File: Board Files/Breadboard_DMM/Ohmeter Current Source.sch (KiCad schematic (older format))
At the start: 18 parts

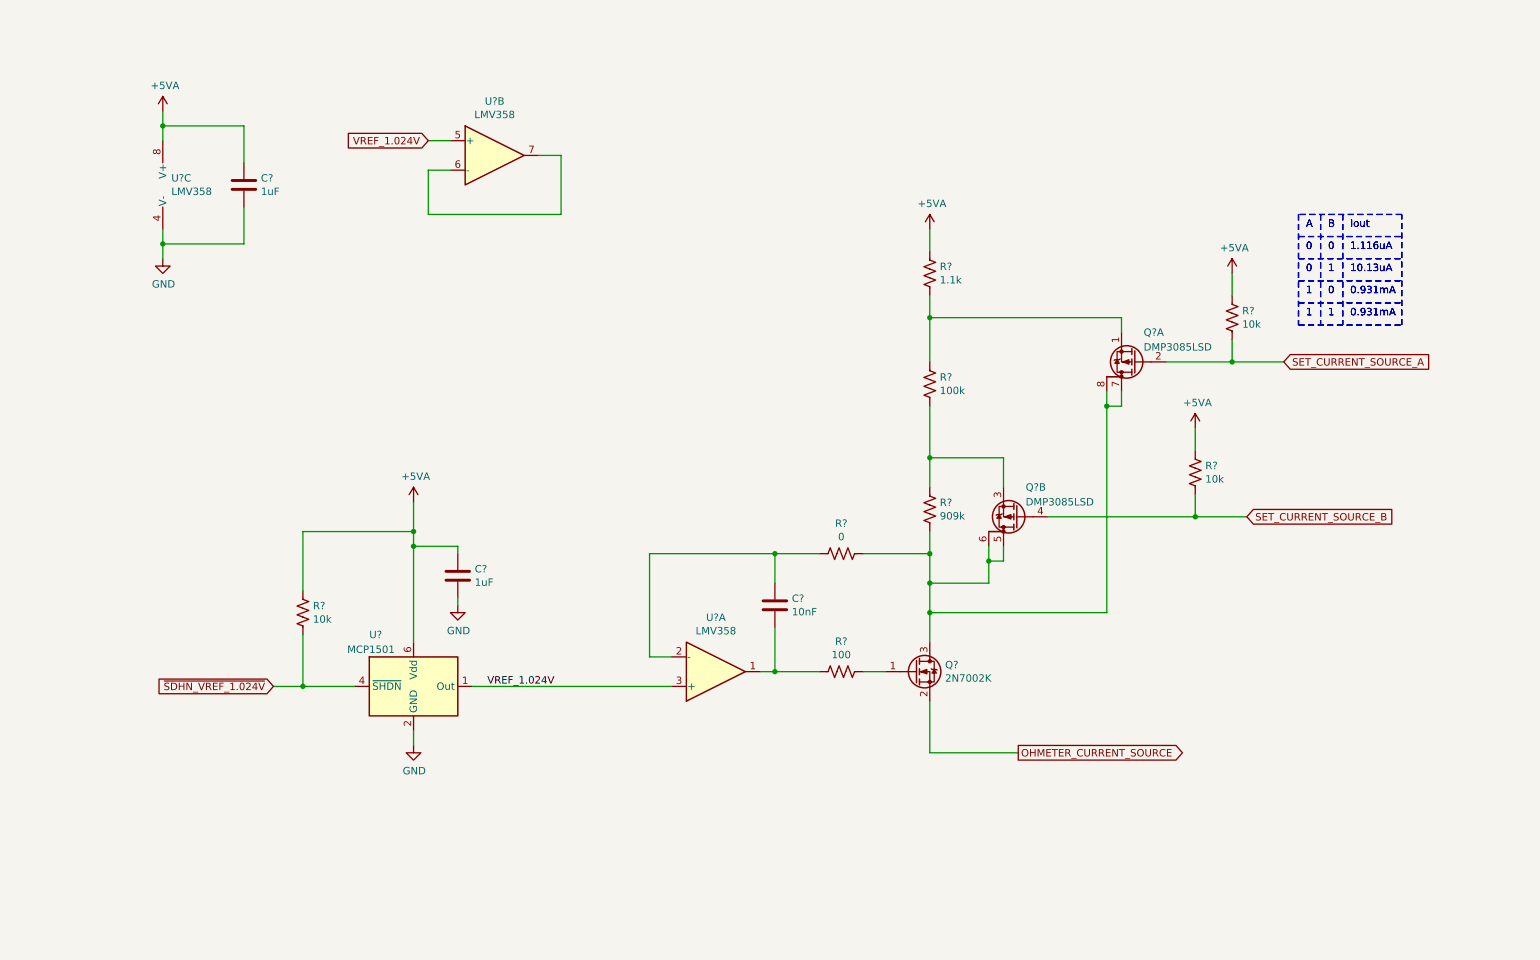
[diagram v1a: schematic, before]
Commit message: Starting converting to hierachichal design
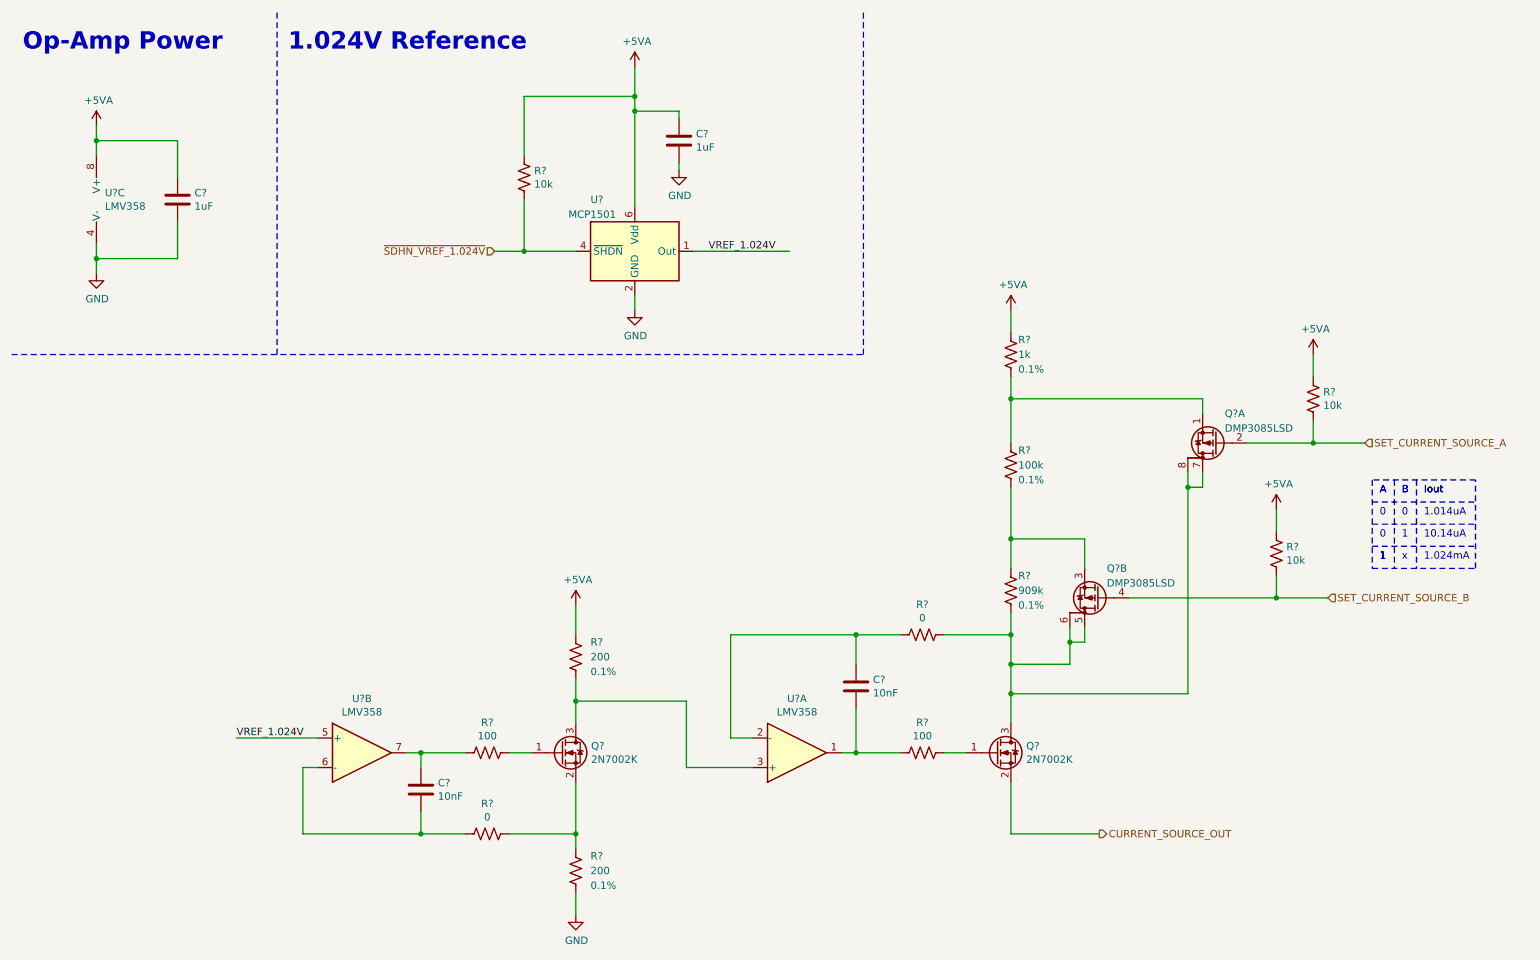
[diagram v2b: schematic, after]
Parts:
- added C?: 10nF, symbol Device:C
- added Q?: 2N7002K, Package_TO_SOT_SMD:SOT-23, symbol Transistor_FET:2N7002K
- added R?: 100, symbol Device:R_US
- added R?: 0, symbol Device:R_US
- added R? (x2): 200, symbol Device:R_US
- R?: value 1.1k -> 1k; Tolerance (none) -> 0.1%
- R? (x2): Tolerance (none) -> 0.1%
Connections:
- net +5VA: now also R?.1
- net GND: now also R?.2
- net VREF_1.024V: no longer U?.3 (+)
- net at U?.6 (-): now also C?.2, R?.2; no longer U?.7
- net OHMETER_CURRENT_SOURCE renamed CURRENT_SOURCE_OUT
- new net: C?.1, R?.2, U?.7
- new net: Q?.3 (D), R?.2, U?.3 (+)
- new net: Q?.1 (G), R?.1
- new net: Q?.2 (S), R?.1, R?.1
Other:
- note added: "1.014uA"
- note added: "1.024V Reference"
- note added: "1.024mA"
- note added: "10.14uA"
- note added: "Op-Amp Power"
- note added: "x"
- note removed: "0.931mA"
- note removed: "1.116uA"
- note removed: "10.13uA"
- moved on the sheet: C?, Q?, Q?A, Q?B, R?, U?, U?A, U?B, U?C

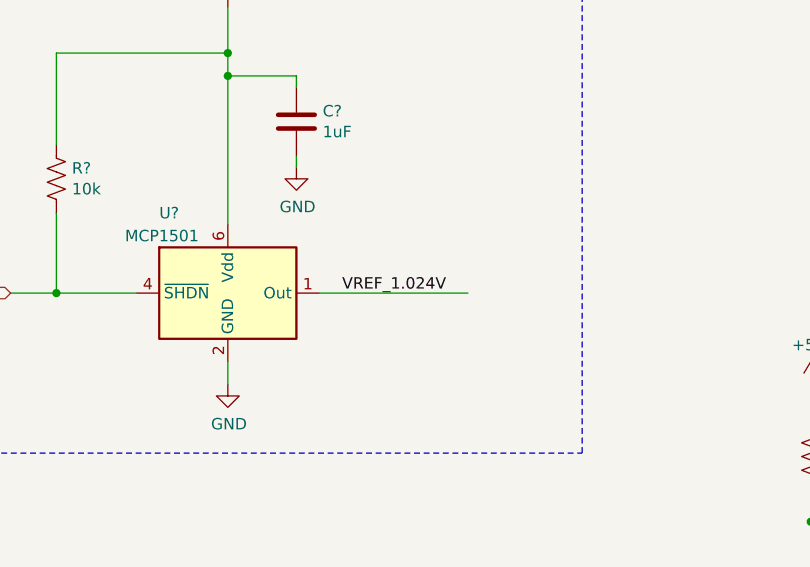
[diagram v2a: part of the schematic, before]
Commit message: Added new sheet for main supply measurement, added upgrades document
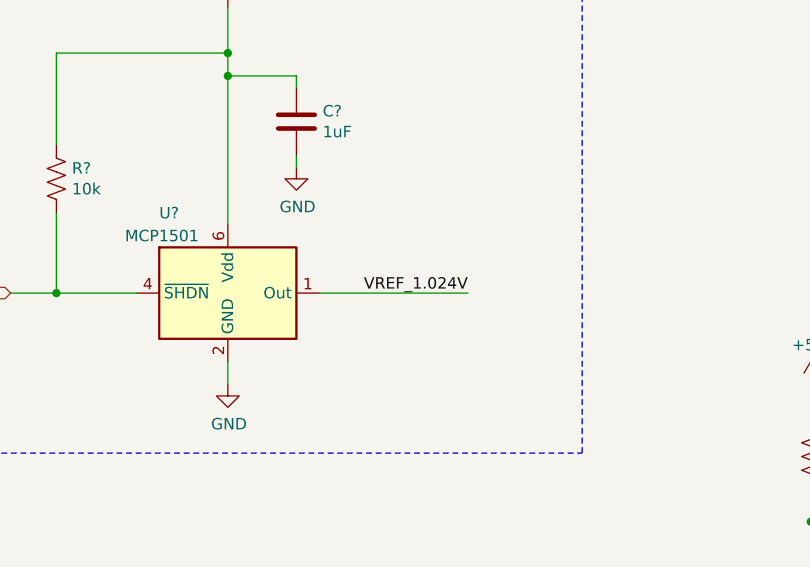
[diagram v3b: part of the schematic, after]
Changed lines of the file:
@@
 AR Path="/5F511849/5F51AF3B" Ref="U?"  Part="3"
 AR Path="/5F5089CB/5F51AF3B" Ref="U?"  Part="3"
+AR Path="/5F7E5DD1/5F51AF3B" Ref="U?"  Part="3"
+AR Path="/5F511849/5F7E68F4/5F51AF3B" Ref="U?"  Part="3"
 F 0 "U?" H 1108 1796 50  0000 L CNN
 F 1 "LMV358" H 1108 1705 50  0000 L CNN
@@
 AR Path="/5F511849/5F51AF41" Ref="C?"  Part="1"
 AR Path="/5F5089CB/5F51AF41" Ref="C?"  Part="1"
+AR Path="/5F7E5DD1/5F51AF41" Ref="C?"  Part="1"
+AR Path="/5F511849/5F7E68F4/5F51AF41" Ref="C?"  Part="1"
 F 0 "C?" H 1715 1796 50  0000 L CNN
 F 1 "1uF" H 1715 1705 50  0000 L CNN
@@
 AR Path="/5F511849/5F51AF4D" Ref="#PWR?"  Part="1"
 AR Path="/5F5089CB/5F51AF4D" Ref="#PWR?"  Part="1"
+AR Path="/5F7E5DD1/5F51AF4D" Ref="#PWR?"  Part="1"
+AR Path="/5F511849/5F7E68F4/5F51AF4D" Ref="#PWR?"  Part="1"
 F 0 "#PWR?" H 1050 1100 50  0001 C CNN
 F 1 "+5VA" H 1065 1423 50  0000 C CNN
@@
 AR Path="/5F511849/5F51AF55" Ref="#PWR?"  Part="1"
 AR Path="/5F5089CB/5F51AF55" Ref="#PWR?"  Part="1"
+AR Path="/5F7E5DD1/5F51AF55" Ref="#PWR?"  Part="1"
+AR Path="/5F511849/5F7E68F4/5F51AF55" Ref="#PWR?"  Part="1"
 F 0 "#PWR?" H 1050 2000 50  0001 C CNN
 F 1 "GND" H 1055 2077 50  0000 C CNN
@@
 AR Path="/5F511849/5F51AF8E" Ref="U?"  Part="1"
 AR Path="/5F5089CB/5F51AF8E" Ref="U?"  Part="1"
+AR Path="/5F7E5DD1/5F51AF8E" Ref="U?"  Part="1"
+AR Path="/5F511849/5F7E68F4/5F51AF8E" Ref="U?"  Part="1"
 F 0 "U?" H 4400 2450 50  0000 L CNN
 F 1 "MCP1501" H 4250 2350 50  0000 L CNN
@@
 AR Path="/5F511849/5F51AF88" Ref="R?"  Part="1"
 AR Path="/5F5089CB/5F51AF88" Ref="R?"  Part="1"
+AR Path="/5F7E5DD1/5F51AF88" Ref="R?"  Part="1"
+AR Path="/5F511849/5F7E68F4/5F51AF88" Ref="R?"  Part="1"
 F 0 "R?" H 4018 1646 50  0000 L CNN
 F 1 "10k" H 4018 1555 50  0000 L CNN
@@
 AR Path="/5F511849/5F51AF7B" Ref="C?"  Part="1"
 AR Path="/5F5089CB/5F51AF7B" Ref="C?"  Part="1"
+AR Path="/5F7E5DD1/5F51AF7B" Ref="C?"  Part="1"
+AR Path="/5F511849/5F7E68F4/5F51AF7B" Ref="C?"  Part="1"
 F 0 "C?" H 5115 1396 50  0000 L CNN
 F 1 "1uF" H 5115 1305 50  0000 L CNN
@@
 AR Path="/5F511849/5F51AF75" Ref="#PWR?"  Part="1"
 AR Path="/5F5089CB/5F51AF75" Ref="#PWR?"  Part="1"
+AR Path="/5F7E5DD1/5F51AF75" Ref="#PWR?"  Part="1"
+AR Path="/5F511849/5F7E68F4/5F51AF75" Ref="#PWR?"  Part="1"
 F 0 "#PWR?" H 4700 2250 50  0001 C CNN
 F 1 "GND" H 4705 2327 50  0000 C CNN
@@
 AR Path="/5F511849/5F51AF6F" Ref="#PWR?"  Part="1"
 AR Path="/5F5089CB/5F51AF6F" Ref="#PWR?"  Part="1"
+AR Path="/5F7E5DD1/5F51AF6F" Ref="#PWR?"  Part="1"
+AR Path="/5F511849/5F7E68F4/5F51AF6F" Ref="#PWR?"  Part="1"
 F 0 "#PWR?" H 5000 1300 50  0001 C CNN
 F 1 "GND" H 5005 1377 50  0000 C CNN
@@
 AR Path="/5F511849/5F51AF64" Ref="#PWR?"  Part="1"
 AR Path="/5F5089CB/5F51AF64" Ref="#PWR?"  Part="1"
+AR Path="/5F7E5DD1/5F51AF64" Ref="#PWR?"  Part="1"
+AR Path="/5F511849/5F7E68F4/5F51AF64" Ref="#PWR?"  Part="1"
 F 0 "#PWR?" H 4700 700 50  0001 C CNN
 F 1 "+5VA" H 4715 1023 50  0000 C CNN
@@
 Wire Wire Line
 	4700 2400 4700 2500
-Text Label 5200 2100 0    50   ~ 0
+Text Label 5750 2100 2    50   ~ 0
 VREF_1.024V
 Wire Wire Line
@@
 AR Path="/5F511849/5F51AFA6" Ref="C?"  Part="1"
 AR Path="/5F5089CB/5F51AFA6" Ref="C?"  Part="1"
+AR Path="/5F7E5DD1/5F51AFA6" Ref="C?"  Part="1"
+AR Path="/5F511849/5F7E68F4/5F51AFA6" Ref="C?"  Part="1"
 F 0 "C?" H 6315 5096 50  0000 L CNN
 F 1 "10nF" H 6315 5005 50  0000 L CNN
@@
 AR Path="/5F511849/5F51AFB7" Ref="R?"  Part="1"
 AR Path="/5F5089CB/5F51AFB7" Ref="R?"  Part="1"
+AR Path="/5F7E5DD1/5F51AFB7" Ref="R?"  Part="1"
+AR Path="/5F511849/5F7E68F4/5F51AFB7" Ref="R?"  Part="1"
 F 0 "R?" V 6445 5500 50  0000 C CNN
 F 1 "100" V 6536 5500 50  0000 C CNN
@@
 AR Path="/5F511849/5F51AFBD" Ref="Q?"  Part="1"
 AR Path="/5F5089CB/5F51AFBD" Ref="Q?"  Part="1"
+AR Path="/5F7E5DD1/5F51AFBD" Ref="Q?"  Part="1"
+AR Path="/5F511849/5F7E68F4/5F51AFBD" Ref="Q?"  Part="1"
 F 0 "Q?" H 7354 5546 50  0000 L CNN
 F 1 "2N7002K" H 7354 5455 50  0000 L CNN
@@
 AR Path="/5F511849/5F51AFCA" Ref="R?"  Part="1"
 AR Path="/5F5089CB/5F51AFCA" Ref="R?"  Part="1"
+AR Path="/5F7E5DD1/5F51AFCA" Ref="R?"  Part="1"
+AR Path="/5F511849/5F7E68F4/5F51AFCA" Ref="R?"  Part="1"
 F 0 "R?" H 7300 3650 50  0000 L CNN
 F 1 "100k" H 7300 3550 50  0000 L CNN
@@
 AR Path="/5F511849/5F51AFD0" Ref="R?"  Part="1"
 AR Path="/5F5089CB/5F51AFD0" Ref="R?"  Part="1"
+AR Path="/5F7E5DD1/5F51AFD0" Ref="R?"  Part="1"
+AR Path="/5F511849/5F7E68F4/5F51AFD0" Ref="R?"  Part="1"
 F 0 "R?" H 7300 4500 50  0000 L CNN
 F 1 "909k" H 7300 4400 50  0000 L CNN
@@
 AR Path="/5F511849/5F51AFDC" Ref="U?"  Part="1"
 AR Path="/5F5089CB/5F51AFDC" Ref="U?"  Part="1"
+AR Path="/5F7E5DD1/5F51AFDC" Ref="U?"  Part="1"
+AR Path="/5F511849/5F7E68F4/5F51AFDC" Ref="U?"  Part="1"
 F 0 "U?" H 5800 5133 50  0000 C CNN
 F 1 "LMV358" H 5800 5224 50  0000 C CNN
@@
 AR Path="/5F511849/5F51AFAC" Ref="R?"  Part="1"
 AR Path="/5F5089CB/5F51AFAC" Ref="R?"  Part="1"
+AR Path="/5F7E5DD1/5F51AFAC" Ref="R?"  Part="1"
+AR Path="/5F511849/5F7E68F4/5F51AFAC" Ref="R?"  Part="1"
 F 0 "R?" V 6445 4700 50  0000 C CNN
 F 1 "0" V 6536 4700 50  0000 C CNN
@@
 U 2 1 5F5655C0
 P 7850 4450
+AR Path="/5F5089CB/5F5655C0" Ref="Q?"  Part="2"
+AR Path="/5F7E5DD1/5F5655C0" Ref="Q?"  Part="2"
+AR Path="/5F511849/5F7E68F4/5F5655C0" Ref="Q?"  Part="2"
 F 0 "Q?" H 7800 4250 50  0000 R CNN
 F 1 "DMP3085LSD" H 7800 4350 50  0000 R CNN
@@
 U 1 1 5F561C46
 P 8650 3400
+AR Path="/5F5089CB/5F561C46" Ref="Q?"  Part="1"
+AR Path="/5F7E5DD1/5F561C46" Ref="Q?"  Part="1"
+AR Path="/5F511849/5F7E68F4/5F561C46" Ref="Q?"  Part="1"
 F 0 "Q?" H 8600 3200 50  0000 R CNN
 F 1 "DMP3085LSD" H 8600 3300 50  0000 R CNN
@@
 AR Path="/5F511849/5F51AFC4" Ref="R?"  Part="1"
 AR Path="/5F5089CB/5F51AFC4" Ref="R?"  Part="1"
+AR Path="/5F7E5DD1/5F51AFC4" Ref="R?"  Part="1"
+AR Path="/5F511849/5F7E68F4/5F51AFC4" Ref="R?"  Part="1"
 F 0 "R?" H 7300 2900 50  0000 L CNN
 F 1 "1k" H 7300 2800 50  0000 L CNN
@@
 AR Path="/5F511849/5F51AF95" Ref="#PWR?"  Part="1"
 AR Path="/5F5089CB/5F51AF95" Ref="#PWR?"  Part="1"
+AR Path="/5F7E5DD1/5F51AF95" Ref="#PWR?"  Part="1"
+AR Path="/5F511849/5F7E68F4/5F51AF95" Ref="#PWR?"  Part="1"
 F 0 "#PWR?" H 7250 2350 50  0001 C CNN
 F 1 "+5VA" H 7265 2673 50  0000 C CNN
@@
 AR Path="/5F511849/5F5A365F" Ref="R?"  Part="1"
 AR Path="/5F5089CB/5F5A365F" Ref="R?"  Part="1"
+AR Path="/5F7E5DD1/5F5A365F" Ref="R?"  Part="1"
+AR Path="/5F511849/5F7E68F4/5F5A365F" Ref="R?"  Part="1"
 F 0 "R?" H 9368 3146 50  0000 L CNN
 F 1 "10k" H 9368 3055 50  0000 L CNN
@@
 AR Path="/5F511849/5F5A469D" Ref="#PWR?"  Part="1"
 AR Path="/5F5089CB/5F5A469D" Ref="#PWR?"  Part="1"
+AR Path="/5F7E5DD1/5F5A469D" Ref="#PWR?"  Part="1"
+AR Path="/5F511849/5F7E68F4/5F5A469D" Ref="#PWR?"  Part="1"
 F 0 "#PWR?" H 9300 2650 50  0001 C CNN
 F 1 "+5VA" H 9315 2973 50  0000 C CNN
@@
 AR Path="/5F511849/5F5A7AF8" Ref="R?"  Part="1"
 AR Path="/5F5089CB/5F5A7AF8" Ref="R?"  Part="1"
+AR Path="/5F7E5DD1/5F5A7AF8" Ref="R?"  Part="1"
+AR Path="/5F511849/5F7E68F4/5F5A7AF8" Ref="R?"  Part="1"
 F 0 "R?" H 9118 4196 50  0000 L CNN
 F 1 "10k" H 9118 4105 50  0000 L CNN
@@
 AR Path="/5F511849/5F5A7B02" Ref="#PWR?"  Part="1"
 AR Path="/5F5089CB/5F5A7B02" Ref="#PWR?"  Part="1"
+AR Path="/5F7E5DD1/5F5A7B02" Ref="#PWR?"  Part="1"
+AR Path="/5F511849/5F7E68F4/5F5A7B02" Ref="#PWR?"  Part="1"
 F 0 "#PWR?" H 9050 3700 50  0001 C CNN
 F 1 "+5VA" H 9065 4023 50  0000 C CNN
@@
 AR Path="/5F511849/5F51AFD6" Ref="U?"  Part="2"
 AR Path="/5F5089CB/5F51AFD6" Ref="U?"  Part="2"
+AR Path="/5F7E5DD1/5F51AFD6" Ref="U?"  Part="2"
+AR Path="/5F511849/5F7E68F4/5F51AFD6" Ref="U?"  Part="2"
 F 0 "U?" H 2850 5867 50  0000 C CNN
 F 1 "LMV358" H 2850 5776 50  0000 C CNN
@@
 AR Path="/5F511849/5F687D36" Ref="C?"  Part="1"
 AR Path="/5F5089CB/5F687D36" Ref="C?"  Part="1"
+AR Path="/5F7E5DD1/5F687D36" Ref="C?"  Part="1"
+AR Path="/5F511849/5F7E68F4/5F687D36" Ref="C?"  Part="1"
 F 0 "C?" H 3365 5796 50  0000 L CNN
 F 1 "10nF" H 3365 5705 50  0000 L CNN
@@
 AR Path="/5F511849/5F687D45" Ref="R?"  Part="1"
 AR Path="/5F5089CB/5F687D45" Ref="R?"  Part="1"
+AR Path="/5F7E5DD1/5F687D45" Ref="R?"  Part="1"
+AR Path="/5F511849/5F7E68F4/5F687D45" Ref="R?"  Part="1"
 F 0 "R?" V 3495 5500 50  0000 C CNN
 F 1 "100" V 3586 5500 50  0000 C CNN
@@
 AR Path="/5F511849/5F687D4F" Ref="Q?"  Part="1"
 AR Path="/5F5089CB/5F687D4F" Ref="Q?"  Part="1"
+AR Path="/5F7E5DD1/5F687D4F" Ref="Q?"  Part="1"
+AR Path="/5F511849/5F7E68F4/5F687D4F" Ref="Q?"  Part="1"
 F 0 "Q?" H 4404 5546 50  0000 L CNN
 F 1 "2N7002K" H 4404 5455 50  0000 L CNN
@@
 AR Path="/5F511849/5F687D5C" Ref="R?"  Part="1"
 AR Path="/5F5089CB/5F687D5C" Ref="R?"  Part="1"
+AR Path="/5F7E5DD1/5F687D5C" Ref="R?"  Part="1"
+AR Path="/5F511849/5F7E68F4/5F687D5C" Ref="R?"  Part="1"
 F 0 "R?" V 3495 6050 50  0000 C CNN
 F 1 "0" V 3586 6050 50  0000 C CNN
@@
 AR Path="/5F511849/5F6BBC43" Ref="R?"  Part="1"
 AR Path="/5F5089CB/5F6BBC43" Ref="R?"  Part="1"
+AR Path="/5F7E5DD1/5F6BBC43" Ref="R?"  Part="1"
+AR Path="/5F511849/5F7E68F4/5F6BBC43" Ref="R?"  Part="1"
 F 0 "R?" H 4400 6400 50  0000 L CNN
 F 1 "200" H 4400 6300 50  0000 L CNN
@@
 AR Path="/5F511849/5F6BEBCD" Ref="#PWR?"  Part="1"
 AR Path="/5F5089CB/5F6BEBCD" Ref="#PWR?"  Part="1"
+AR Path="/5F7E5DD1/5F6BEBCD" Ref="#PWR?"  Part="1"
+AR Path="/5F511849/5F7E68F4/5F6BEBCD" Ref="#PWR?"  Part="1"
 F 0 "#PWR?" H 4300 6350 50  0001 C CNN
 F 1 "GND" H 4305 6427 50  0000 C CNN
@@
 AR Path="/5F511849/5F6E67BD" Ref="R?"  Part="1"
 AR Path="/5F5089CB/5F6E67BD" Ref="R?"  Part="1"
+AR Path="/5F7E5DD1/5F6E67BD" Ref="R?"  Part="1"
+AR Path="/5F511849/5F7E68F4/5F6E67BD" Ref="R?"  Part="1"
 F 0 "R?" H 4400 4950 50  0000 L CNN
 F 1 "200" H 4400 4850 50  0000 L CNN
@@
 AR Path="/5F511849/5F6E715F" Ref="#PWR?"  Part="1"
 AR Path="/5F5089CB/5F6E715F" Ref="#PWR?"  Part="1"
+AR Path="/5F7E5DD1/5F6E715F" Ref="#PWR?"  Part="1"
+AR Path="/5F511849/5F7E68F4/5F6E715F" Ref="#PWR?"  Part="1"
 F 0 "#PWR?" H 4300 4350 50  0001 C CNN
 F 1 "+5VA" H 4315 4673 50  0000 C CNN

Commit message: Finished main design, cleaning up schematic
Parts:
- removed C?: 10nF, symbol Device:C
- removed Q? (x2): 2N7002K, Package_TO_SOT_SMD:SOT-23, symbol Transistor_FET:2N7002K
- removed Q? (x2): DMP3085LSD, Package_SO:SO-8_3.9x4.9mm_P1.27mm, symbol irex_Transistor_FET:DMP3085LSD
- removed R? (x2): 100, symbol Device:R_US
- removed R?: 0, symbol Device:R_US
- removed R? (x2): 200, symbol Device:R_US
- added D?: DF2B7AFU, Diode_SMD:D_SOD-323_HandSoldering, symbol Device:D_TVS_ALT
- added Q? (x4): NTZD3154N, Package_TO_SOT_SMD:SOT-563, symbol irex_Transistor_FET:NTZD3154N
- added R?: 10k, symbol Device:R_US
- added R? (x2): 1k, symbol Device:R_US
- R?: value 0 -> 10k
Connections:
- net +5VA: no longer R?.1
- net GND: now also R?.2, Q?.1 (S1), Q?.4 (S2)
- net SET_CURRENT_SOURCE_A: now also Q?.2 (G1)
- net SET_CURRENT_SOURCE_B: now also Q?.5 (G2)
- net VREF_1.024V: now also R?.2
- net at R?.2, U?.2 (-): now also C?.2; no longer C?.1
- net at U?.1: now also C?.1, D?.1 (A1), Q?.3 (D2), Q?.6 (D1), R?.2; no longer C?.2
- net CURRENT_SOURCE_OUT-: now reaches R?.1
- net CURRENT_SOURCE_OUT-: now also R?.1, Q?.1 (S1), Q?.4 (S2), R?.1; no longer R?.2
- net at R?.1, R?.2: now also Q?.6 (D1)
- net at R?.1, R?.2: now also Q?.3 (D2)
- net at U?.6 (-): now also U?.7
- net at U?.3 (+): now also R?.1
- net ~SDHN_VREF_1.024V~: no longer names the net of R?.2, U?.4 (~SHDN~)
- new net: D?.2 (A2), Q?.2 (G1), Q?.5 (G2), R?.2
- new net CURRENT_SOURCE_OUT+: R?.1
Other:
- note added: "Op-Amp Termination"
- note added: "Over voltage protection"
- moved on the sheet: C?, R?, U?, U?A, U?B
